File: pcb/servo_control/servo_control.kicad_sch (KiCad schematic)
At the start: 59 parts, among them J1 Jack-DC, J10 Conn_01x03_Female, J11 Conn_01x03_Female, J12 Conn_01x03_Female, J13 Conn_01x03_Female, J14 Conn_01x03_Female, J15 Conn_01x03_Female, J16 Conn_01x03_Female, J17 Conn_01x03_Female, J18 Conn_01x03_Female, J19 Conn_01x03_Female, J2 YLIDAR X4, J20 Conn_01x03_Female, J21 Conn_01x06_Male, J22 GY-87, J3 Conn_01x03_Female, J4 Conn_01x03_Female, J5 Conn_01x03_Female, J6 Conn_01x03_Female, J7 Conn_01x03_Female, J8 Conn_01x03_Female, J9 Conn_01x03_Female, SW1 ESP_PROG, SW2 ESP_RST, U1 PCA9685BS, U2 LM317-3.3_SOT-223, U3 ESP32-WROOM-32, U4 MCP73213-A6SI/MF, U5 PCA9685BS, U6 LM317-5_SOT-223, U7 LT1085-ADJ

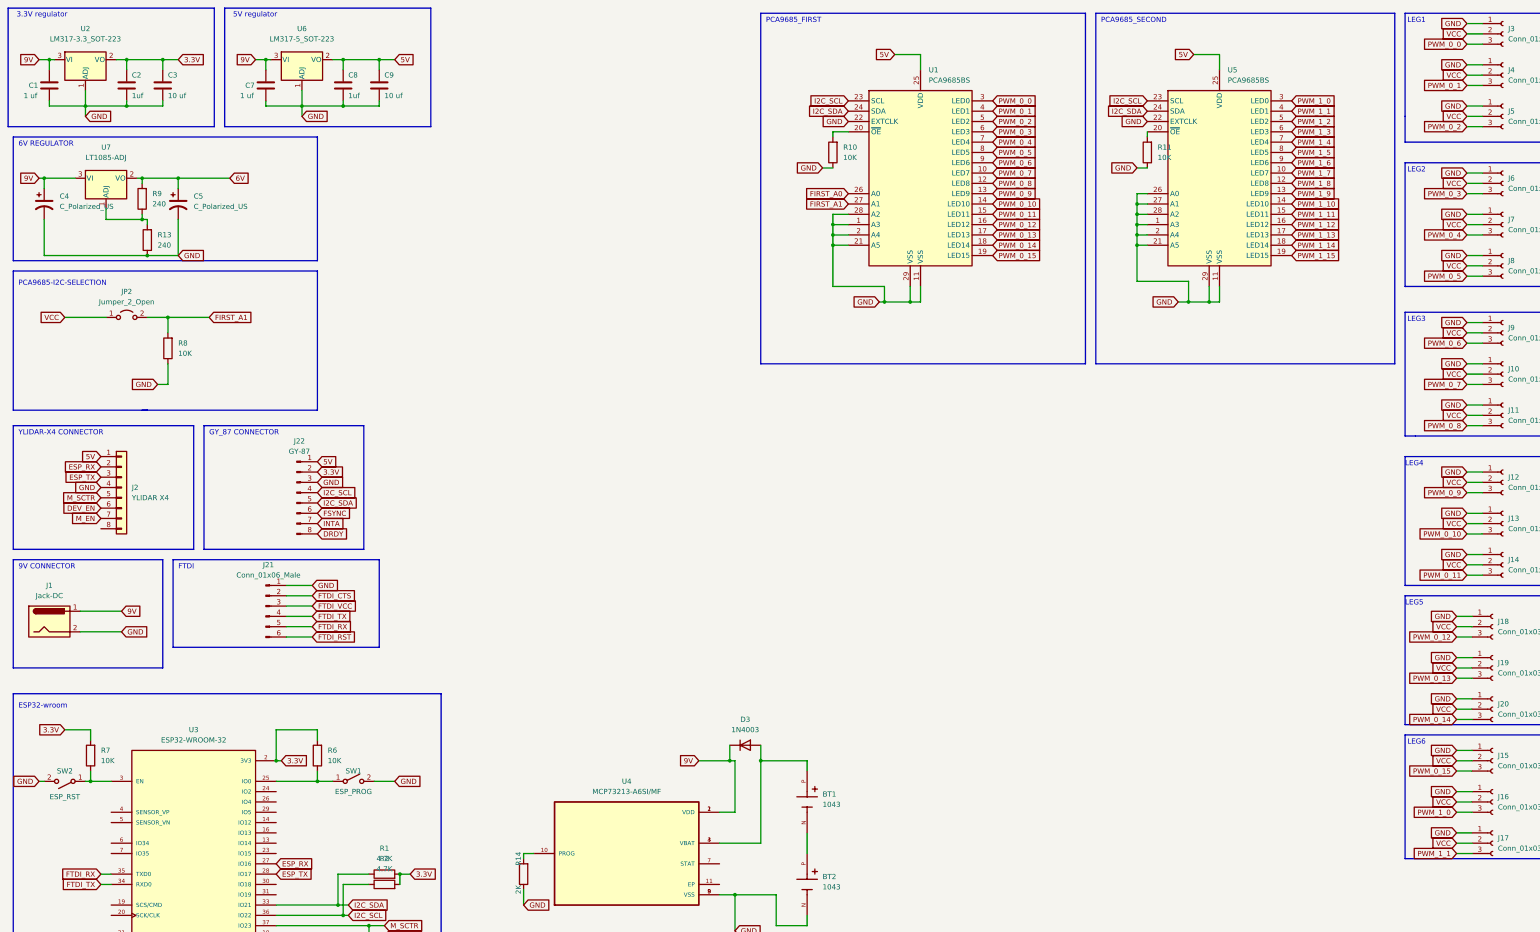
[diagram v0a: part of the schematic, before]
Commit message: add 6V regulator
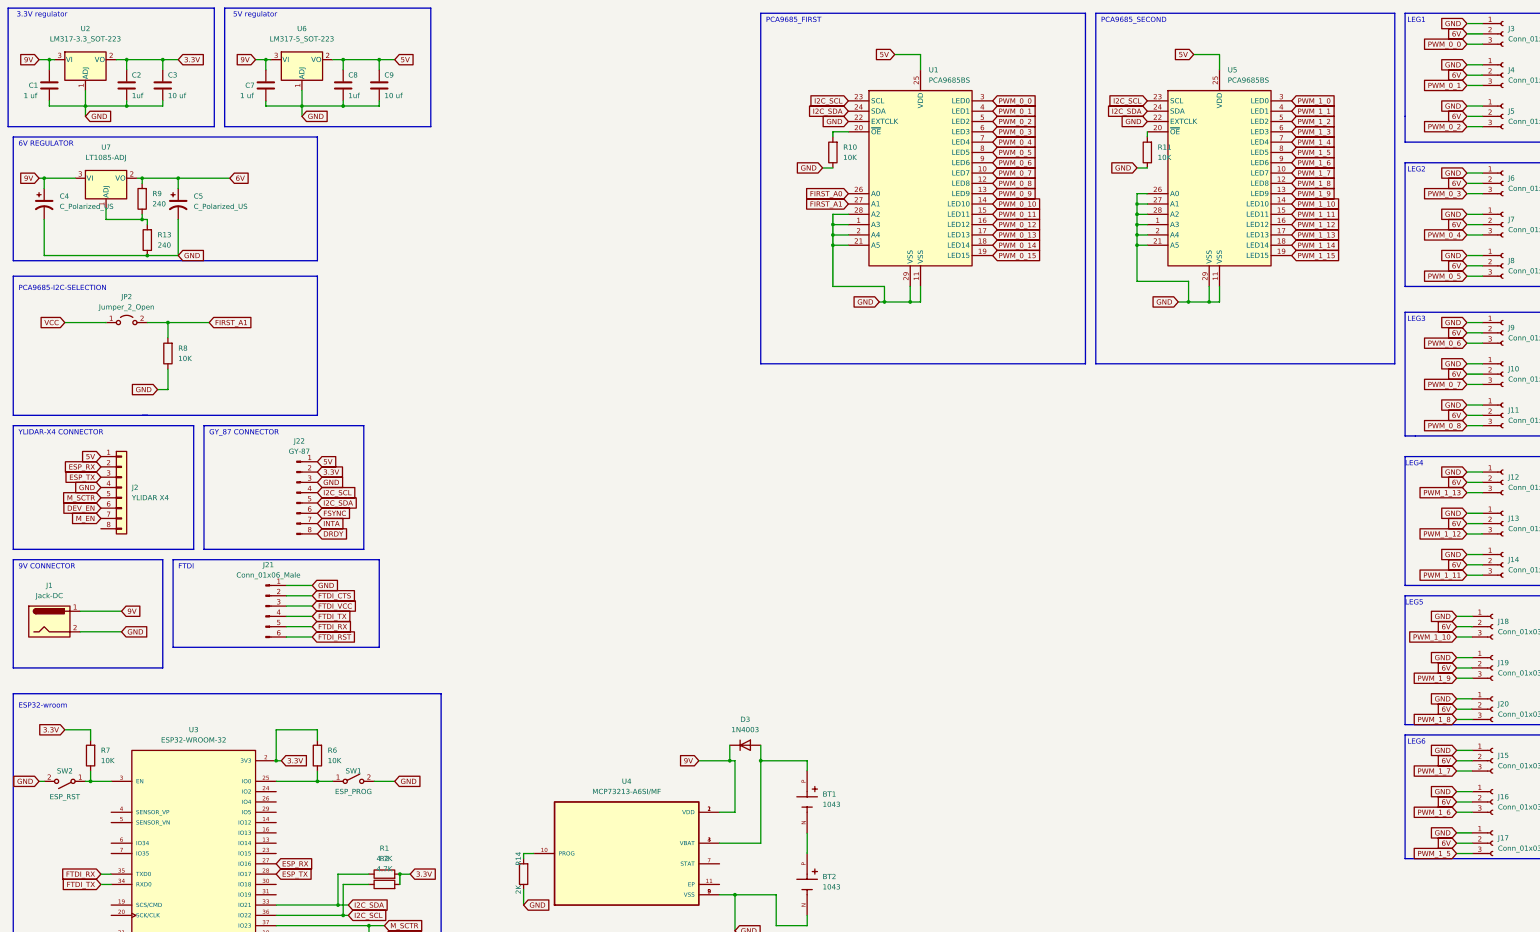
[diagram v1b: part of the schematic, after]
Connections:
- net 6V: now also J10.2 (Pin_2), J11.2 (Pin_2), J12.2 (Pin_2), J13.2 (Pin_2), J14.2 (Pin_2), J15.2 (Pin_2), J16.2 (Pin_2), J17.2 (Pin_2), J18.2 (Pin_2), J19.2 (Pin_2), J20.2 (Pin_2), J3.2 (Pin_2), J4.2 (Pin_2), J5.2 (Pin_2), J6.2 (Pin_2), J7.2 (Pin_2), J8.2 (Pin_2), J9.2 (Pin_2)
- net PWM_0_10: no longer J13.3 (Pin_3)
- net PWM_0_11: no longer J14.3 (Pin_3)
- net PWM_0_12: no longer J18.3 (Pin_3)
- net PWM_0_13: no longer J19.3 (Pin_3)
- net PWM_0_14: no longer J20.3 (Pin_3)
- net PWM_0_15: no longer J15.3 (Pin_3)
- net PWM_0_9: no longer J12.3 (Pin_3)
- net PWM_1_0: no longer J16.3 (Pin_3)
- net PWM_1_1: no longer J17.3 (Pin_3)
- net PWM_1_10: now also J18.3 (Pin_3)
- net PWM_1_11: now also J14.3 (Pin_3)
- net PWM_1_12: now also J13.3 (Pin_3)
- net PWM_1_13: now also J12.3 (Pin_3)
- net PWM_1_5: now also J17.3 (Pin_3)
- net PWM_1_6: now also J16.3 (Pin_3)
- net PWM_1_7: now also J15.3 (Pin_3)
- net PWM_1_8: now also J20.3 (Pin_3)
- net PWM_1_9: now also J19.3 (Pin_3)
- net VCC: no longer J10.2 (Pin_2), J11.2 (Pin_2), J12.2 (Pin_2), J13.2 (Pin_2), J14.2 (Pin_2), J15.2 (Pin_2), J16.2 (Pin_2), J17.2 (Pin_2), J18.2 (Pin_2), J19.2 (Pin_2), J20.2 (Pin_2), J3.2 (Pin_2), J4.2 (Pin_2), J5.2 (Pin_2), J6.2 (Pin_2), J7.2 (Pin_2), J8.2 (Pin_2), J9.2 (Pin_2)
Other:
- moved on the sheet: JP2, R8

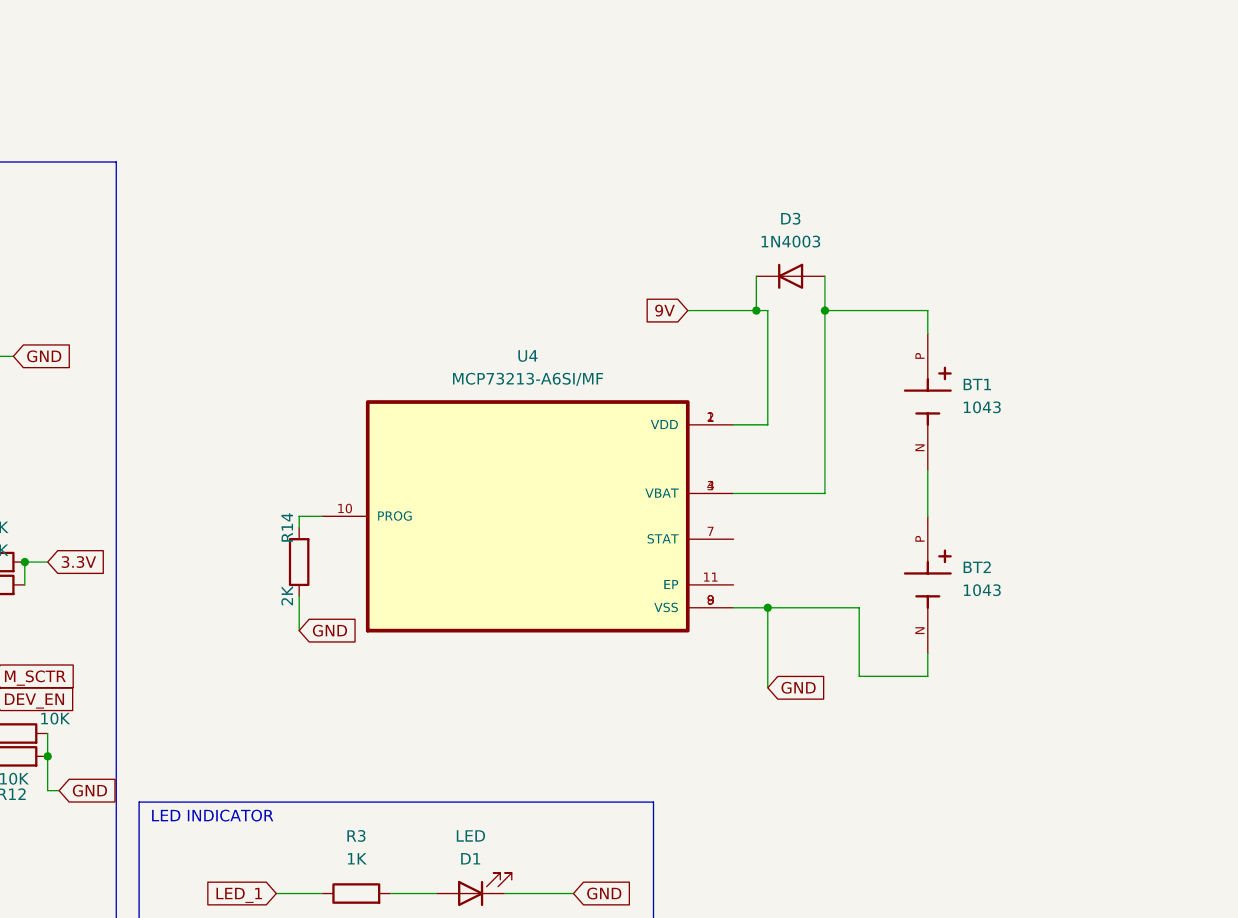
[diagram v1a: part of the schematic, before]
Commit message: add MCP73213
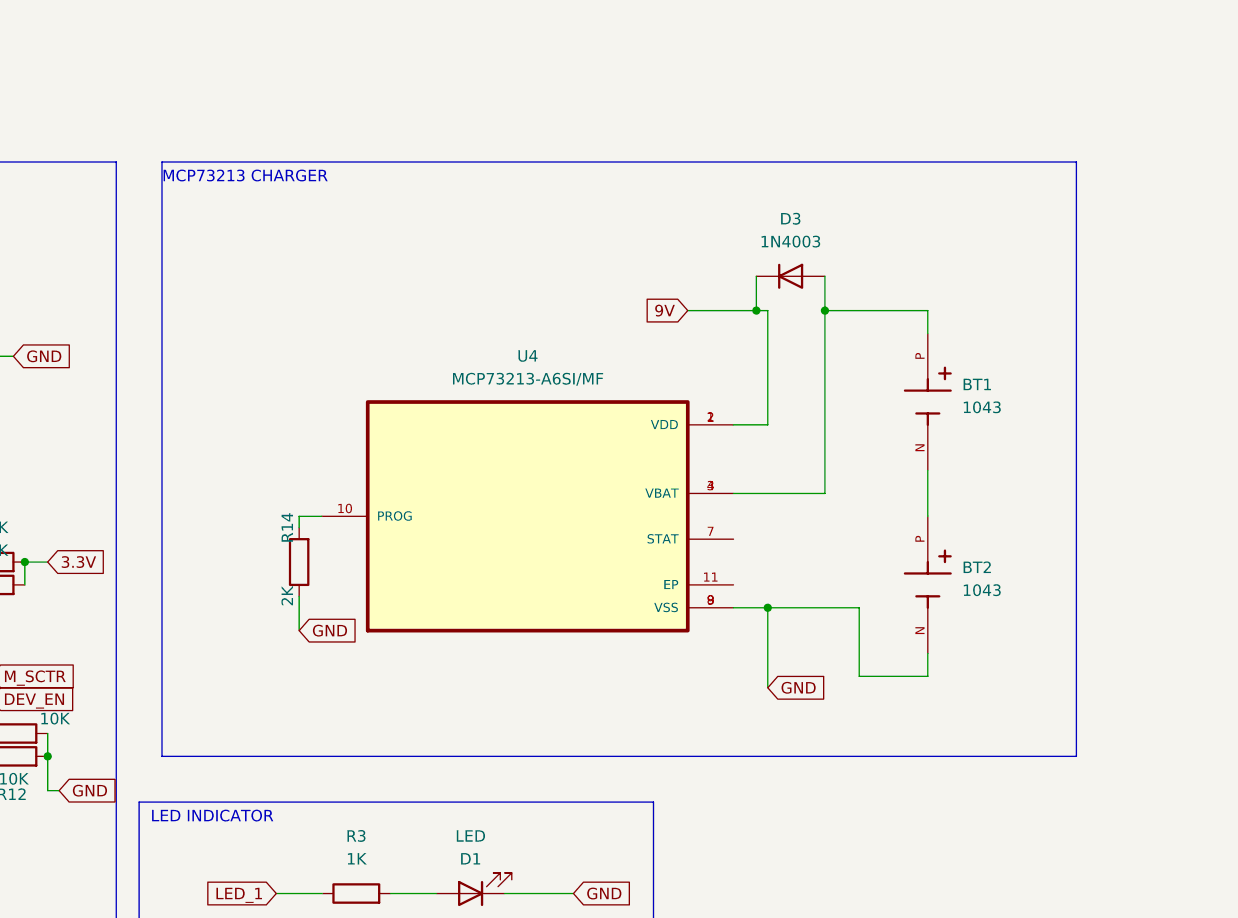
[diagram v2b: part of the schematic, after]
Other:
- note added: "MCP73213 CHARGER"
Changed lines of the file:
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@@
+    (stroke (width 0) (type default) (color 0 0 0 0))
+  )
+  (polyline (pts (xy 227.33 248.92) (xy 125.73 248.92))
     (stroke (width 0) (type default) (color 0 0 0 0))
   )
@@
     (stroke (width 0) (type default) (color 0 0 0 0))
   )
+  (polyline (pts (xy 227.33 182.88) (xy 227.33 248.92))
+    (stroke (width 0) (type default) (color 0 0 0 0))
+  )
+  (polyline (pts (xy 125.73 182.88) (xy 227.33 182.88))
+    (stroke (width 0) (type default) (color 0 0 0 0))
+  )
   (polyline (pts (xy 123.19 254) (xy 123.19 278.13))
     (stroke (width 0) (type default) (color 0 0 0 0))
@@
     (stroke (width 0) (type default) (color 0 0 0 0))
   )
+  (polyline (pts (xy 125.73 182.88) (xy 125.73 248.92))
+    (stroke (width 0) (type default) (color 0 0 0 0))
+  )
   (wire (pts (xy 373.38 27.94) (xy 377.19 27.94))
     (stroke (width 0) (type default) (color 0 0 0 0))
@@
     (effects (font (size 1.27 1.27)) (justify left bottom))
   )
+  (text "MCP73213 CHARGER\n" (at 125.73 185.42 0)
+    (effects (font (size 1.27 1.27)) (justify left bottom))
+  )

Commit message: finish pcb
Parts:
- added D4: LED, LED_SMD:LED_0603_1608Metric, symbol Device:LED
- added R15: 10K, Resistor_SMD:R_0603_1608Metric, symbol Device:R
- added R16: 1K, Resistor_SMD:R_0603_1608Metric, symbol Device:R
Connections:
- net VCC is gone; now on net 5V: JP2.1 (A)
- net 9V: now also R16.2
- net GND: now also R15.2
- net M_EN: now also U3.11 (IO26), R15.1
- net at U4.7 (STAT): now also D4.1 (K)
- new net: D4.2 (A), R16.1
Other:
- moved on the sheet: BT1, BT2

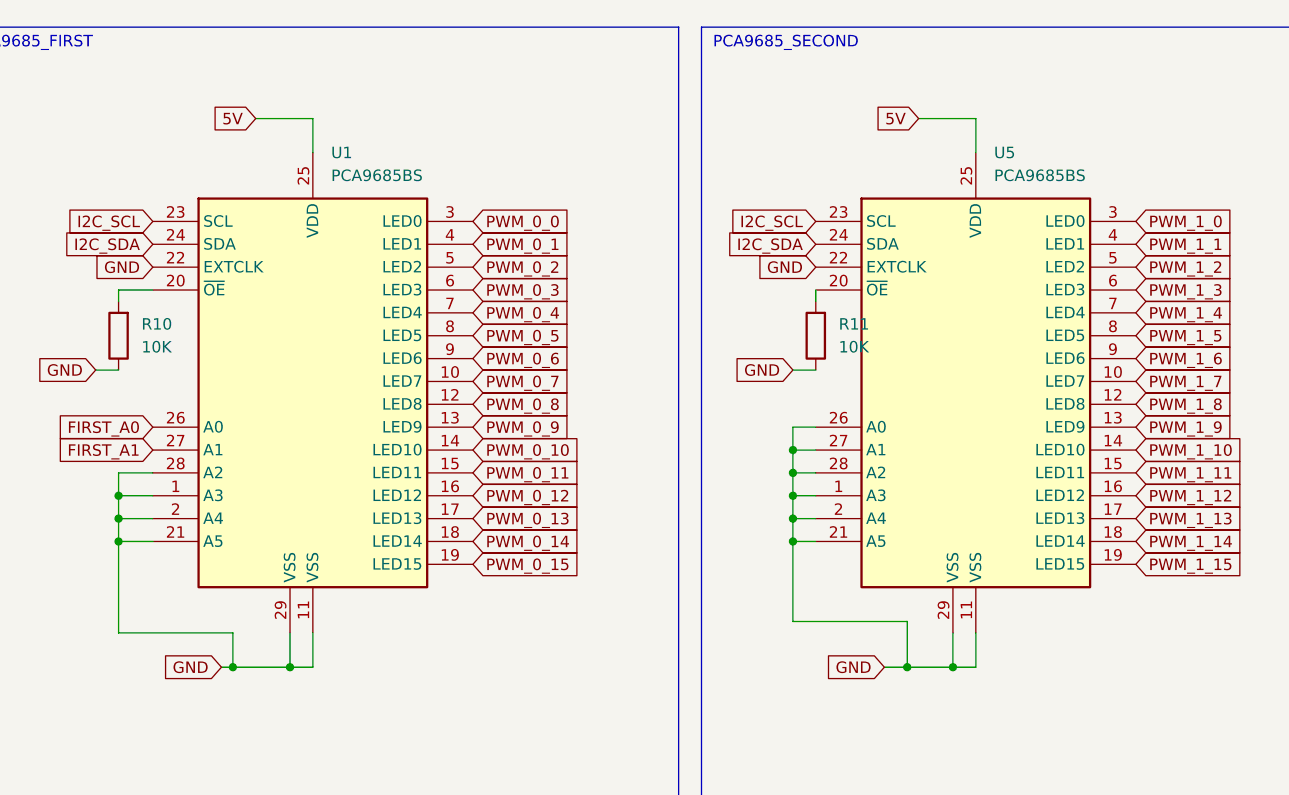
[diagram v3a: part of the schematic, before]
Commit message: fix PCA9685 footprint
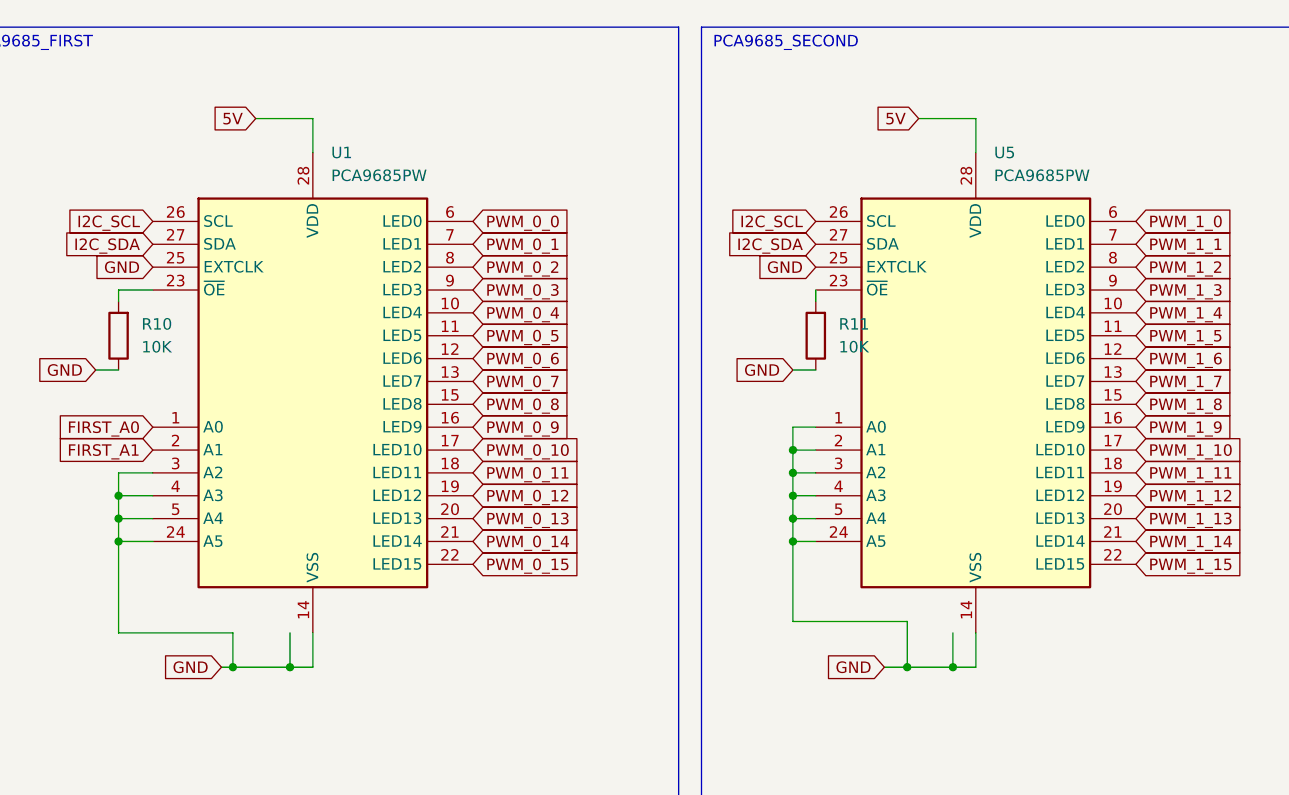
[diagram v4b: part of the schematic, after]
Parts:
- removed U1, U5: PCA9685BS, Package_SO:HTSSOP-28-1EP_4.4x9.7mm_P0.65mm_EP3.4x9.5mm, symbol Driver_LED:PCA9685BS
- added U1, U5: PCA9685PW, Package_SO:TSSOP-28_4.4x9.7mm_P0.65mm, symbol Driver_LED:PCA9685PW
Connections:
- net 5V: now also U1.28 (VDD), U5.28 (VDD)
- net FIRST_A0: now also U1.1 (A0)
- net FIRST_A1: now also U1.2 (A1)
- net GND: now also U1.14 (VSS), U1.24 (A5), U1.25 (EXTCLK), U1.3 (A2), U1.4 (A3), U1.5 (A4), U5.1 (A0), U5.14 (VSS), U5.2 (A1), U5.24 (A5), U5.25 (EXTCLK), U5.3 (A2), U5.4 (A3), U5.5 (A4)
- net I2C_SCL: now also U1.26 (SCL), U5.26 (SCL)
- net I2C_SDA: now also U1.27 (SDA), U5.27 (SDA)
- net PWM_0_0: now also U1.6 (LED0)
- net PWM_0_1: now also U1.7 (LED1)
- net PWM_0_10: now also U1.17 (LED10)
- net PWM_0_11: now also U1.18 (LED11)
- net PWM_0_12: now also U1.19 (LED12)
- net PWM_0_13: now also U1.20 (LED13)
- net PWM_0_14: now also U1.21 (LED14)
- net PWM_0_15: now also U1.22 (LED15)
- net PWM_0_2: now also U1.8 (LED2)
- net PWM_0_3: now also U1.9 (LED3)
- net PWM_0_4: now also U1.10 (LED4)
- net PWM_0_5: now also U1.11 (LED5)
- net PWM_0_6: now also U1.12 (LED6)
- net PWM_0_7: now also U1.13 (LED7)
- net PWM_0_8: now also U1.15 (LED8)
- net PWM_0_9: now also U1.16 (LED9)
- net PWM_1_0: now also U5.6 (LED0)
- net PWM_1_1: now also U5.7 (LED1)
- net PWM_1_10: now also U5.17 (LED10)
- net PWM_1_11: now also U5.18 (LED11)
- net PWM_1_12: now also U5.19 (LED12)
- net PWM_1_13: now also U5.20 (LED13)
- net PWM_1_14: now also U5.21 (LED14)
- net PWM_1_15: now also U5.22 (LED15)
- net PWM_1_2: now also U5.8 (LED2)
- net PWM_1_3: now also U5.9 (LED3)
- net PWM_1_4: now also U5.10 (LED4)
- net PWM_1_5: now also U5.11 (LED5)
- net PWM_1_6: now also U5.12 (LED6)
- net PWM_1_7: now also U5.13 (LED7)
- net PWM_1_8: now also U5.15 (LED8)
- net PWM_1_9: now also U5.16 (LED9)
- net at R11.2: now also U5.23 (~{OE})
- net at R10.2: now also U1.23 (~{OE})
